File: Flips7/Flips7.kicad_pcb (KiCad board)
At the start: 2 copper layers, 100 x 100 mm, 16 parts, among them CN1 Conn_02x17_Odd_Even, CN2 Conn_02x17_Odd_Even, U1 FP2800A, U2 FP2800A, U3 FP2800A

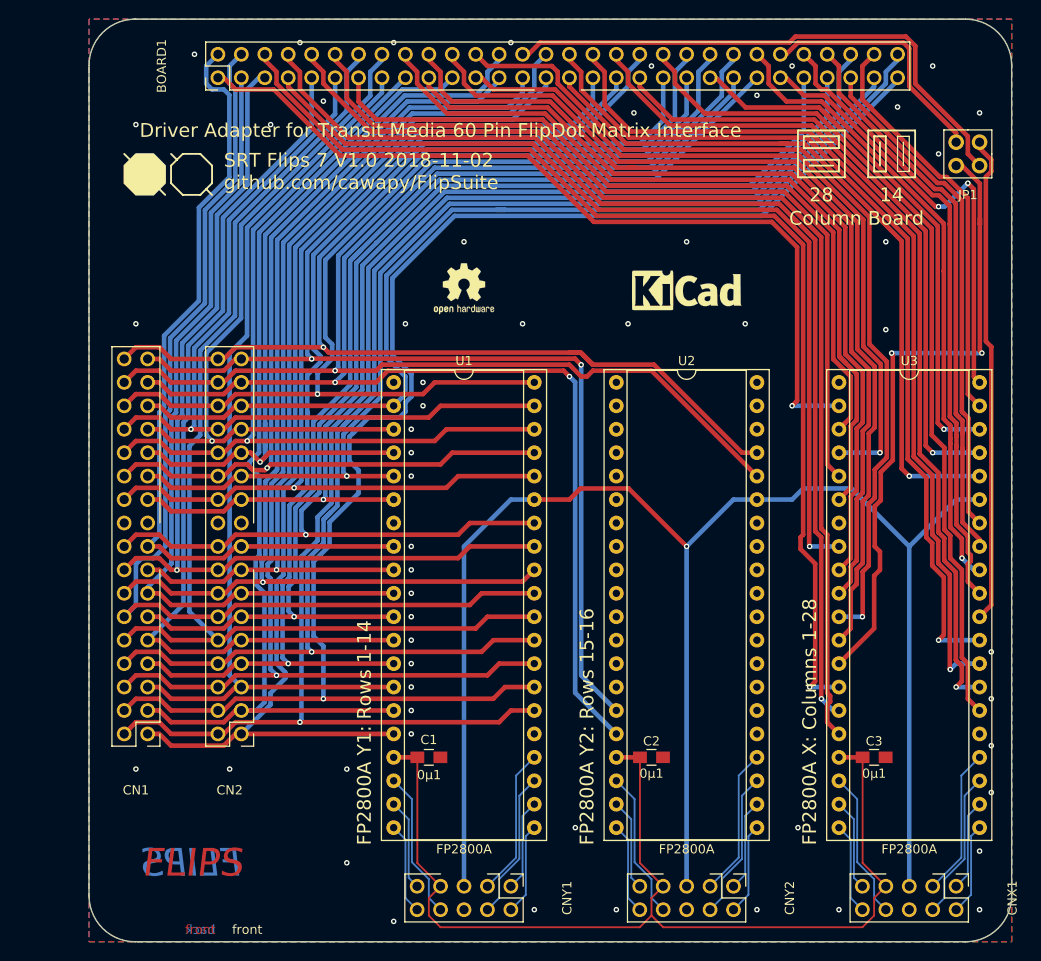
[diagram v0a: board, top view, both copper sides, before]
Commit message: Shifting board connector to get space for mounting pads
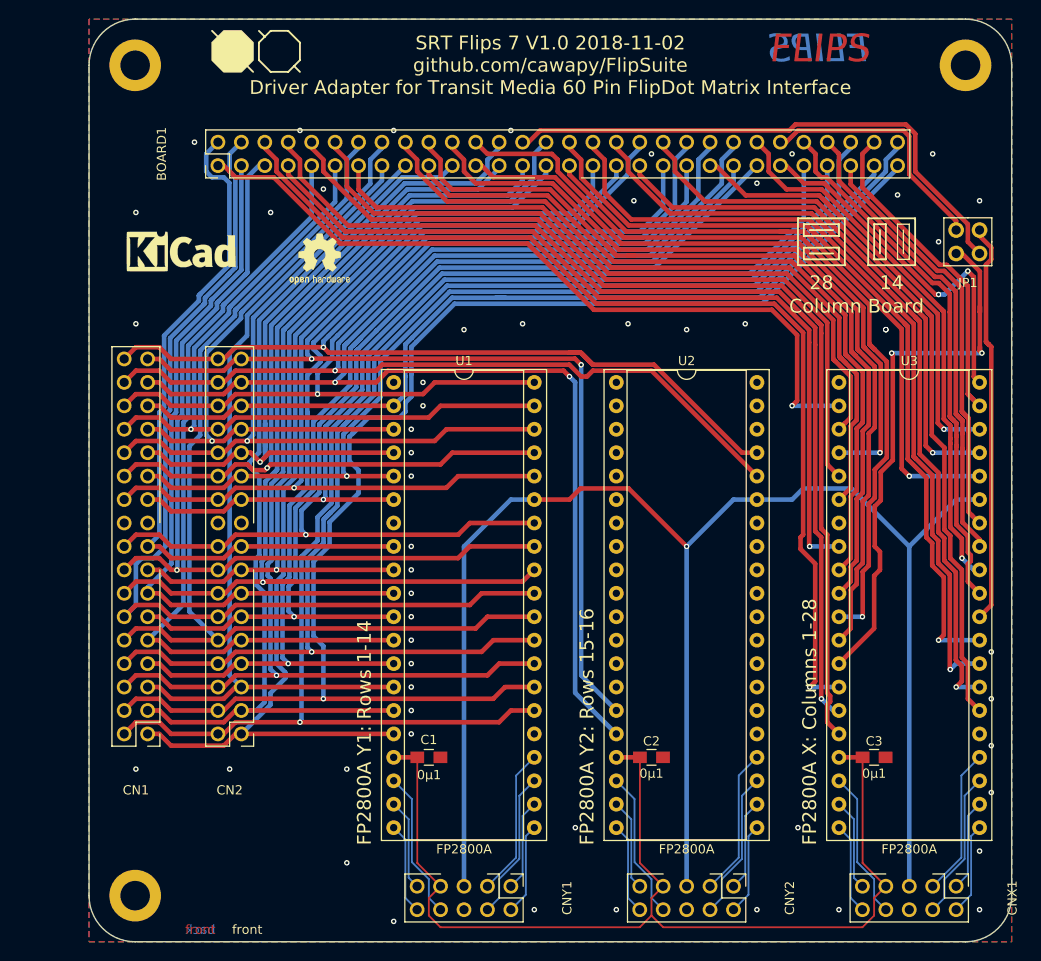
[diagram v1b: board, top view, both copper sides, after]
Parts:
- added REF**: MountingHole_3.2mm_M3_DIN965_Pad, Mounting_Holes:MountingHole_3.2mm_M3_DIN965_Pad, F.Cu at (30.4, 120.4)
- added REF**: MountingHole_3.2mm_M3_DIN965_Pad, Mounting_Holes:MountingHole_3.2mm_M3_DIN965_Pad, F.Cu at (120.4, 30.4)
- added REF**: MountingHole_3.2mm_M3_DIN965_Pad, Mounting_Holes:MountingHole_3.2mm_M3_DIN965_Pad, F.Cu at (30.4, 30.4)
- moved REF** 54.9 mm to (35.4, 50.4)
- moved REF*** 16.0 mm to (50.4, 51.4)
- moved BOARD1 9.52 mm to (39.4, 41.3)
- moved JP1 9.52 mm to (121.9, 48.3)
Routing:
- net /~SY11: track 110.7 -> 99.4 mm
- net /RY09: track 165.3 -> 154.1 mm
- net /RY04: track 111.7 -> 101.6 mm
- net /RY16: track 140.0 -> 130.1 mm
- net /RY08: track 159.6 -> 150.1 mm
- net /~SY16: track 145.3 -> 135.8 mm
- net /~SY10: track 90.9 -> 81.4 mm
- net /~SY08: track 114.5 -> 105.0 mm
- net /~SY05: track 121.3 -> 111.8 mm
- net /~SY03: track 101.1 -> 91.6 mm
- net /~SY02: track 110.8 -> 101.3 mm
- net /~SY01: track 125.2 -> 115.7 mm
- net /RY15: track 140.8 -> 131.2 mm
- net /RY11: track 157.7 -> 148.1 mm
- net /RY03: track 93.0 -> 83.5 mm
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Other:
- board text added: "SRT Flips 7 V1.0 2018-11-02 github.com/cawapy/FlipSuite Driver Adapter for Transit Media 60 Pin FlipDot Matrix Interface"
- board text removed: "Driver Adapter for Transit Media 60 Pin FlipDot Matrix Interface"
- board text removed: "SRT Flips 7 V1.0 2018-11-02 github.com/cawapy/FlipSuite"

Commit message: Improve tracing
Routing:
- net /~SY10: track 81.4 -> 76.2 mm
- net /~SY16: track 135.8 -> 139.6 mm, vias 2 -> 1
- net /~SY15: track 146.5 -> 148.8 mm, vias 2 -> 1
- net /~SY02: track 101.3 -> 99.3 mm
- net /RY15: track 131.2 -> 133.1 mm, vias 1 -> 2
- net /RY06: track 81.9 -> 83.4 mm
- net /RY16: track 130.1 -> 128.7 mm
- net /~SY07: track 78.6 -> 79.7 mm
- net /RY11: track 148.1 -> 149.2 mm
- net /~SY04: track 114.4 -> 113.6 mm
- net /~SY12: track 77.8 -> 78.6 mm
- net /RY07: track 95.1 -> 95.7 mm
- net /HV: vias 1 -> 0
- net /GND: vias 54 -> 65

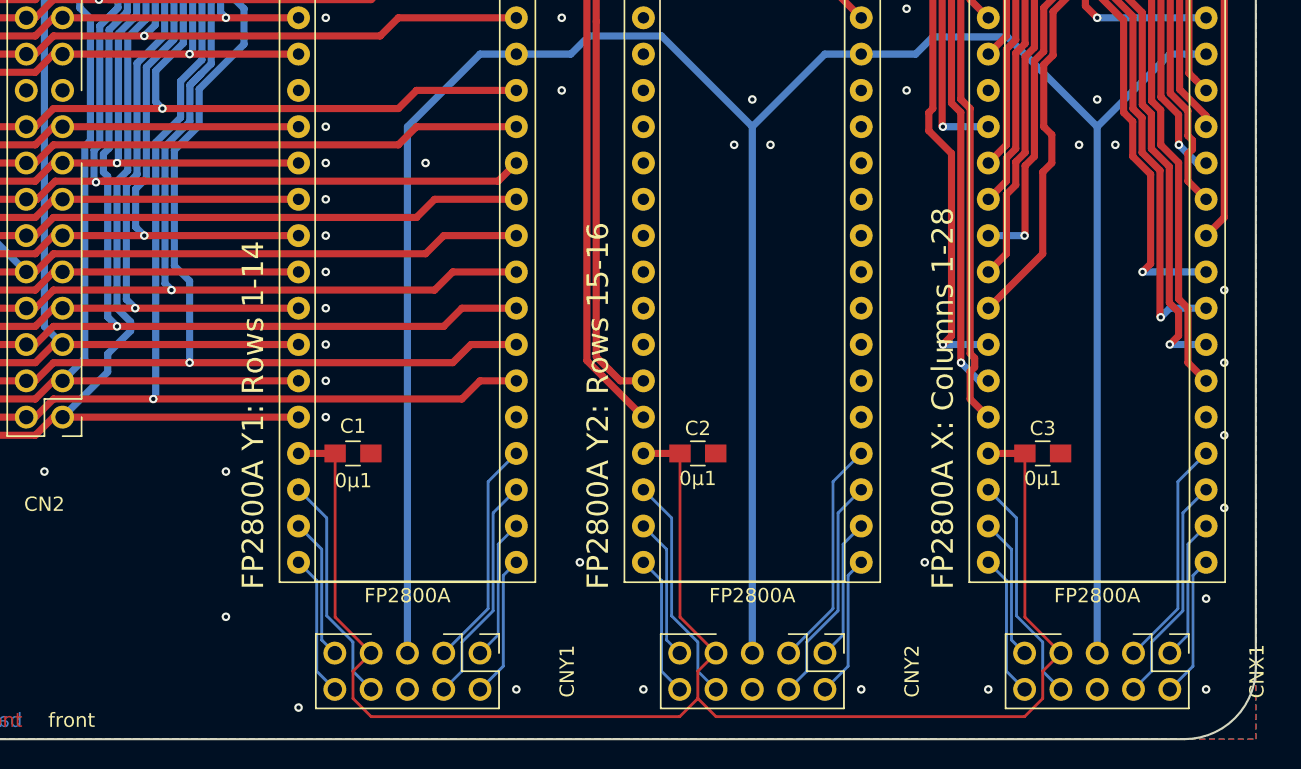
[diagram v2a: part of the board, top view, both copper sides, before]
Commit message: moving connectors and adding 4th mounting pad
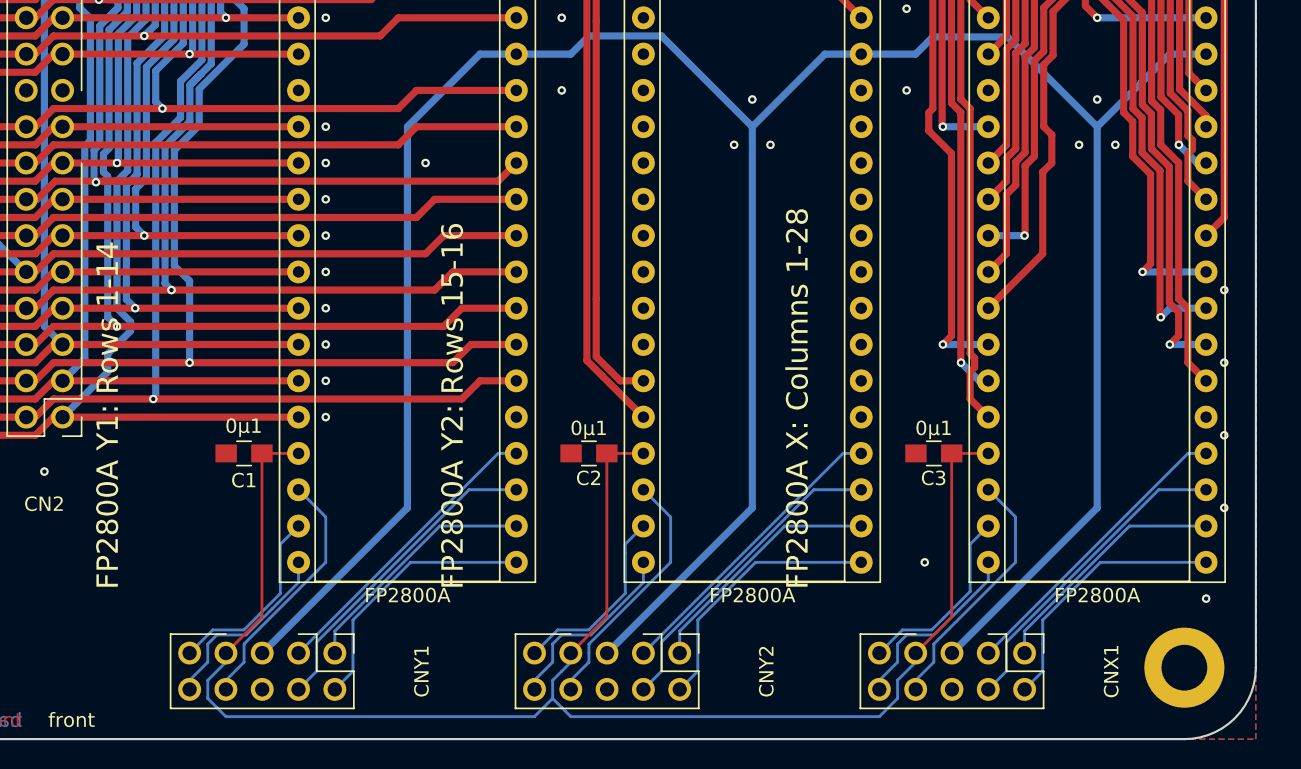
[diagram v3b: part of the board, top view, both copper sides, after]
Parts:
- added REF**: MountingHole_3.2mm_M3_DIN965_Pad, Mounting_Holes:MountingHole_3.2mm_M3_DIN965_Pad, F.Cu at (120.4, 120.4)
- moved CNY1 10.2 mm to (61.0, 119.4)
- moved CNX1 10.2 mm to (109.2, 119.4)
- moved CNY2 10.2 mm to (85.1, 119.4)
- moved C2 7.62 mm to (78.7, 105.4), turned to 180 degrees
- moved C1 7.62 mm to (54.6, 105.4), turned to 0 degrees
- moved C3 7.62 mm to (102.9, 105.4), turned to 180 degrees
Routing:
- net /HV: track 178.9 -> 191.6 mm
- net /X.B0: track 9.94 -> 18.5 mm
- net /R.B0: track 9.94 -> 18.5 mm
- net /L.B0: track 9.94 -> 18.5 mm
- net /L.B1: track 9.94 -> 17.3 mm
- net /X.B1: track 9.94 -> 17.3 mm
- net /R.B1: track 9.94 -> 17.3 mm
- net /R.POL: track 16.1 -> 22.2 mm
- net /X.POL: track 16.1 -> 22.2 mm
- net /L.POL: track 16.1 -> 22.2 mm
- net /R.EN: track 16.1 -> 21.0 mm
- net /X.EN: track 16.1 -> 21.0 mm
- net /L.EN: track 16.1 -> 21.0 mm
- net /L.A0: track 9.94 -> 13.3 mm
- net /R.A0: track 9.94 -> 13.3 mm
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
